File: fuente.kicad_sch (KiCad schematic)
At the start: 13 parts

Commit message: avance en SCH
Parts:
- added D1: SM4007, Diode_SMD:D_MELF, symbol Diode:SM4007
- added TP1: TP5V, TestPoint:TestPoint_Loop_D2.50mm_Drill1.0mm, symbol Connector:TestPoint
- added TP2: TP3V3, TestPoint:TestPoint_Loop_D2.50mm_Drill1.0mm, symbol Connector:TestPoint
- C4: renamed from C?; footprint (none) -> Capacitor_SMD:CP_Elec_6.3x7.7
- L1: renamed from L?; footprint (none) -> Inductor_THT:L_Radial_D7.5mm_P5.00mm_Fastron_07P
- gave numbers to parts that had none: 11
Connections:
- net +5V: now also C6.1, U2.3 (VI), TP1.1
- net at C2.1, C3.1, U1.1 (VIN): now also D1.1 (K)
- net +3V3: now reaches C7.1, U2.2 (VO)
- net +3V3: now also TP2.1
- new net VIN: D1.2 (A)

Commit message: avance en PCB y SCH
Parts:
- D1: footprint Diode_SMD:D_MELF -> Diode_SMD:D_SMA_Handsoldering
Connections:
- net +VSW: now reaches C2.1, C3.1, D1.1 (K), U1.1 (VIN)
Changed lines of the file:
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@@
   (junction (at 123.19 91.44) (diameter 0) (color 0 0 0 0)
   )
+  (junction (at 114.3 74.93) (diameter 0) (color 0 0 0 0)
+  )
   (junction (at 96.52 91.44) (diameter 0) (color 0 0 0 0)
   )
@@
     (stroke (width 0) (type default) (color 0 0 0 0))
   )
+  (wire (pts (xy 114.3 74.93) (xy 124.46 74.93))
+    (stroke (width 0) (type default) (color 0 0 0 0))
+  )
   (wire (pts (xy 137.16 91.44) (xy 158.75 91.44))
     (stroke (width 0) (type default) (color 0 0 0 0))
@@
     (stroke (width 0) (type default) (color 0 0 0 0))
   )
-  (wire (pts (xy 106.68 74.93) (xy 124.46 74.93))
+  (wire (pts (xy 106.68 74.93) (xy 114.3 74.93))
     (stroke (width 0) (type default) (color 0 0 0 0))
   )
@@
     (stroke (width 0) (type default) (color 0 0 0 0))
   )
+  (wire (pts (xy 114.3 68.58) (xy 114.3 74.93))
+    (stroke (width 0) (type default) (color 0 0 0 0))
+  )
   (wire (pts (xy 151.13 134.62) (xy 151.13 135.89))
     (stroke (width 0) (type default) (color 0 0 0 0))
@@
   )
   (wire (pts (xy 120.65 125.73) (xy 120.65 127))
+    (stroke (width 0) (type default) (color 0 0 0 0))
+  )
+  (wire (pts (xy 116.84 68.58) (xy 114.3 68.58))
     (stroke (width 0) (type default) (color 0 0 0 0))
   )
@@
   )
   (hierarchical_label "3.3V" (shape output) (at 171.45 125.73 0)
+    (effects (font (size 1.27 1.27)) (justify left))
+  )
+  (hierarchical_label "+VSW" (shape output) (at 116.84 68.58 0)
     (effects (font (size 1.27 1.27)) (justify left))
   )
@@
     (property "Reference" "D1" (id 0) (at 87.63 68.58 0))
     (property "Value" "SM4007" (id 1) (at 87.63 71.12 0))
-    (property "Footprint" "Diode_SMD:D_MELF" (id 2) (at 87.63 70.485 0)
+    (property "Footprint" "Diode_SMD:D_SMA_Handsoldering" (id 2) (at 87.63 70.485 0)
       (effects (font (size 1.27 1.27)) hide)
     )
@@
       (effects (font (size 1.27 1.27)) hide)
     )
+    (pin "1")
+  )
+  (symbol (lib_id "power:+VSW") (at 106.68 74.93 0) (unit 1)
+    (in_bom yes) (on_board yes) (fields_autoplaced)
+    (property "Reference" "#PWR0101" (id 0) (at 106.68 78.74 0)
+      (effects (font (size 1.27 1.27)) hide)
+    )
+    (property "Value" "+VSW" (id 1) (at 106.68 69.85 0))
+    (property "Footprint" "" (id 2) (at 106.68 74.93 0)
+      (effects (font (size 1.27 1.27)) hide)
+    )
+    (property "Datasheet" "" (id 3) (at 106.68 74.93 0)
+      (effects (font (size 1.27 1.27)) hide)
+    )

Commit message: avance en PCB y SCH
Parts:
- U2: footprint Package_TO_SOT_SMD:TO-252-3_TabPin2 -> Package_TO_SOT_SMD:SOT-223-3_TabPin2
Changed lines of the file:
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@@
     (property "Reference" "U2" (id 0) (at 137.16 118.11 0))
     (property "Value" "LM1117-3.3" (id 1) (at 137.16 120.65 0))
-    (property "Footprint" "Package_TO_SOT_SMD:TO-252-3_TabPin2" (id 2) (at 137.16 125.73 0)
+    (property "Footprint" "Package_TO_SOT_SMD:SOT-223-3_TabPin2" (id 2) (at 137.16 125.73 0)
       (effects (font (size 1.27 1.27)) hide)
     )

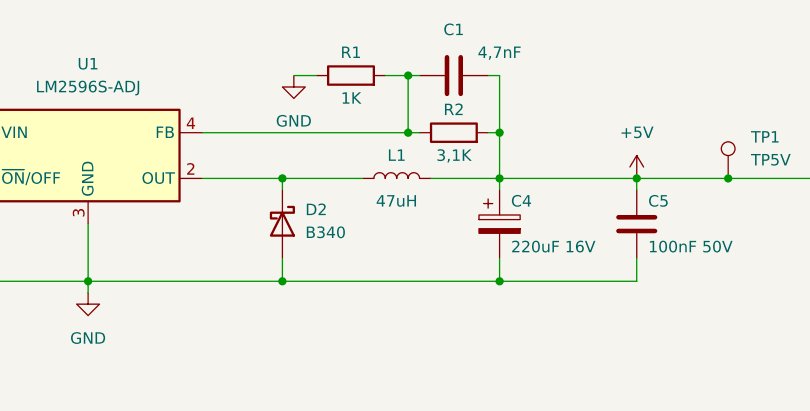
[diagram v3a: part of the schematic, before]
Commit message: cambios menores en valores de componentes
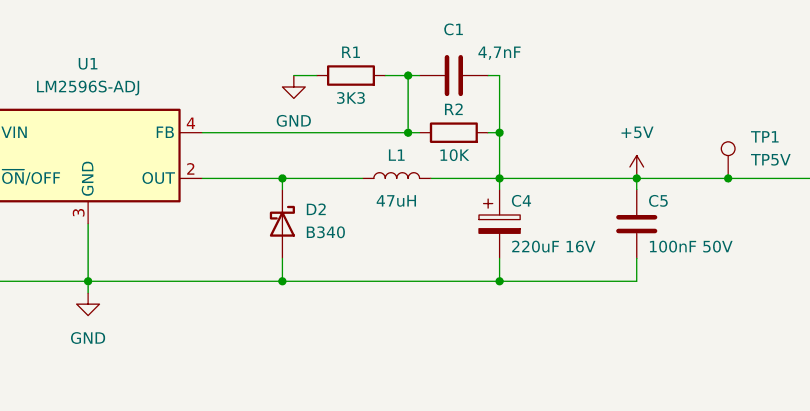
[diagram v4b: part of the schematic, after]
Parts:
- R1: value 1K -> 3K3
- R2: value 3,1K -> 10K
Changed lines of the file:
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@@
     (in_bom yes) (on_board yes)
     (property "Reference" "R2" (id 0) (at 177.8 72.39 90))
-    (property "Value" "3,1K" (id 1) (at 177.8 77.47 90))
+    (property "Value" "10K" (id 1) (at 177.8 77.47 90))
     (property "Footprint" "Resistor_SMD:R_0805_2012Metric_Pad1.20x1.40mm_HandSolder" (id 2) (at 177.8 76.708 90)
       (effects (font (size 1.27 1.27)) hide)
@@
     (in_bom yes) (on_board yes)
     (property "Reference" "R1" (id 0) (at 166.37 66.04 90))
-    (property "Value" "1K" (id 1) (at 166.37 71.12 90))
+    (property "Value" "3K3" (id 1) (at 166.37 71.12 90))
     (property "Footprint" "Resistor_SMD:R_0805_2012Metric_Pad1.20x1.40mm_HandSolder" (id 2) (at 166.37 70.358 90)
       (effects (font (size 1.27 1.27)) hide)
